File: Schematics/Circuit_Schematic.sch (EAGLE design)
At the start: 38 parts, among them Q1 L7812ACV, U1 TDA2822M, X1 1502_01

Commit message: added proper eagle parts for ram and custom part for DAC
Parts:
- removed 23LC1024: (no value), TDA2822D_Breakout:MA04-2
- removed UDA1334ATS: (no value), TDA2822D_Breakout:MA08-2
- added U2: 23LC1024-I/SN, microchip_fromOneCall:23LC1024-I/SN
- added UDA1334ATS/N2_ALEX1: UDA1334ATS/N2_ALEX, UDA1334ATS_ALEX:UDA1334ATS/N2_ALEX
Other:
- note added: "RAM"
- note removed: "RAM for DAC"
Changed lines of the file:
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@@
 <part name="R1" library="SparkFun-Resistors" deviceset="1OHM" device="-0603-1/10W-1%" value="300"/>
 <part name="S1" library="switch" deviceset="255SB" device=""/>
-<part name="UDA1334ATS" library="TDA2822D_Breakout" deviceset="MA08-2" device=""/>
-<part name="23LC1024" library="TDA2822D_Breakout" deviceset="MA04-2" device=""/>
+<part name="U2" library="microchip_fromOneCall" deviceset="23LC1024-I/SN" device=""/>
+<part name="UDA1334ATS/N2_ALEX1" library="UDA1334ATS_ALEX" deviceset="UDA1334ATS/N2_ALEX" device=""/>
 </parts>
 <sheets>
@@
 <text x="83.82" y="175.26" size="1.778" layer="91">3.3V Regulator</text>
 <text x="-15.24" y="-12.7" size="1.778" layer="91">3.3V</text>
-<text x="12.7" y="58.42" size="1.778" layer="91">DAC</text>
-<text x="48.26" y="58.42" size="1.778" layer="91">RAM for DAC</text>
+<text x="0" y="-43.18" size="1.778" layer="91">DAC</text>
+<text x="68.58" y="-45.72" size="1.778" layer="91">RAM</text>
 </plain>
 <instances>
@@
 <instance part="R1" gate="G$1" x="43.18" y="167.64" rot="R90"/>
 <instance part="S1" gate="1" x="5.08" y="187.96" rot="R270"/>
-<instance part="UDA1334ATS" gate="G$1" x="15.24" y="43.18"/>
-<instance part="23LC1024" gate="G$1" x="53.34" y="50.8"/>
+<instance part="U2" gate="A" x="81.28" y="-63.5"/>
+<instance part="UDA1334ATS/N2_ALEX1" gate="G$1" x="0" y="-50.8"/>
 </instances>
 <busses>

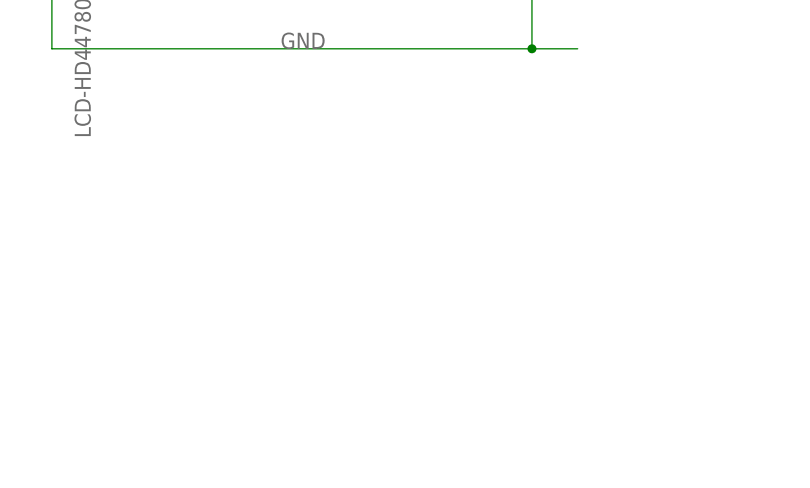
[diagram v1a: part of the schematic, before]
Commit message: Added EEPROM Chip 24C64
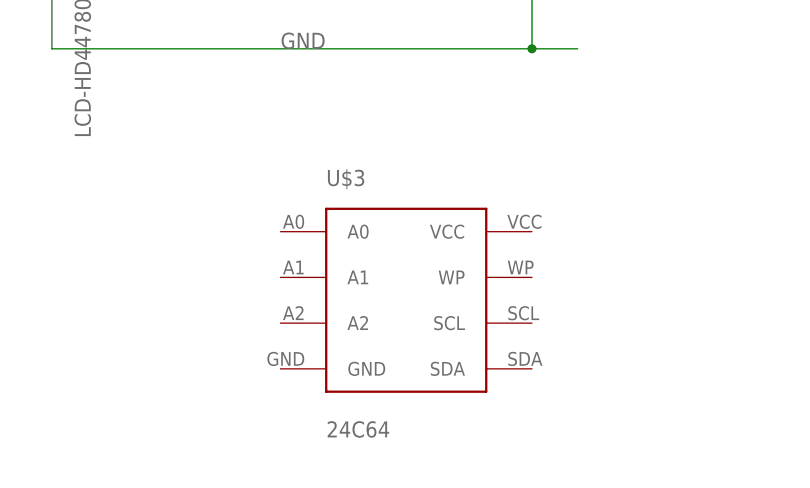
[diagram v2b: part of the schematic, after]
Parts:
- added U$3: 24C64, MIRO:24C64
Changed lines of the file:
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@@
 <part name="U2" library="microchip_fromOneCall" deviceset="23LC1024-I/SN" device=""/>
 <part name="UDA1334ATS/N2_ALEX1" library="UDA1334ATS_ALEX" deviceset="UDA1334ATS/N2_ALEX" device=""/>
+<part name="U$3" library="MIRO" deviceset="24C64" device=""/>
 </parts>
 <sheets>
@@
 <instance part="U2" gate="A" x="81.28" y="-63.5"/>
 <instance part="UDA1334ATS/N2_ALEX1" gate="G$1" x="0" y="-50.8"/>
+<instance part="U$3" gate="G$1" x="137.16" y="-81.28"/>
 </instances>
 <busses>

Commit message: Added ESP controls via NMOS transistors. Lil bit messy.
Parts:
- added T1, T2, T3, T4, T5: (no value), zetex:NMOSSOT223
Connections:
- removed net RD0: U$1.RD0/SEG0, U$2.DB0
- removed net RD1: U$1.RD1/SEG1, U$2.DB1
- new net N$22: MDL1.GPIO5, T1.G
- new net N$23: MDL1.GPIO4, T2.G
- new net N$26: MDL1.GPIO9, T3.G
- new net N$32: MDL1.GPIO12, T5.G
- net GND: now also T1.S, T2.S, T3.S, T4.S, T5.S
- net N$19: now also T2.D, U$1.RB1/INT1/SEG8; no longer U$1.RB5/KBI1
- net N$28: now also MDL1.GPIO10, T4.G; no longer U$1.RB1/INT1/SEG8, U$2.E
- net N$3: now also T5.D, U$1.RG1/TX2/CK2/SEG29; no longer U$1.RA0/AN0
- net N$33: now also T3.D
- net N$8: now also T1.D
- net VDD: now also T4.D, U$1.RG2/RX2/DT2/SEG28; no longer U$1.RA1/AN1
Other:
- note added: "Mute: RB0"
- note added: "Next Channel: RB1"
- note added: "Prev Channel: RB2"
- note added: "Vol Down: RB1"
- note added: "Vol Up: RB0"
- moved on the sheet: MDL1

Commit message: Added AR1010 chip to the schematic, got rid of the breakout for it
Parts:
- removed AR1010_BRKT: (no value), con-lstb:MA07-1
- added U$4: AR1010, MIRO:AR1010
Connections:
- removed net N$2: AR1010_BRKT.1, Q1.OUT
- removed net N$21: MDL1.VCC
- new net VCC: MDL1.VCC, U$4.VCC
- net CLOCK: now also U$4.SCL; no longer AR1010_BRKT.6
- net DATA: now also U$4.SDA; no longer AR1010_BRKT.7_DATA
- net GND: now also U$4.GND; no longer AR1010_BRKT.2
- net N$10: now also U$4.L-OUT; no longer AR1010_BRKT.3
- net N$13: now also U$4.R-OUT; no longer AR1010_BRKT.4
- net VDD: now also Q1.OUT
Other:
- note removed: "CLOCK"
- note removed: "DATA"
- note removed: "GND"
- note removed: "LEFT"
- note removed: "RIGHT"
- note removed: "VSS"
- note removed: "W/R"
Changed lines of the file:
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@@
 </classes>
 <parts>
-<part name="AR1010_BRKT" library="con-lstb" deviceset="MA07-1" device=""/>
 <part name="U1" library="ST Microelctronics_By_element14_Batch_1" deviceset="TDA2822M" device=""/>
 <part name="U$1" library="Microchip_By_element14_Batch_1" deviceset="PIC18F6490-I/PT" device=""/>
@@
 <part name="T4" library="zetex" deviceset="NMOSSOT223" device=""/>
 <part name="T5" library="zetex" deviceset="NMOSSOT223" device=""/>
+<part name="U$4" library="MIRO" deviceset="AR1010" device=""/>
 </parts>
 <sheets>
 <sheet>
 <plain>
-<text x="5.08" y="86.36" size="1.778" layer="91">DATA</text>
-<text x="5.08" y="83.82" size="1.778" layer="91">CLOCK</text>
-<text x="5.08" y="81.28" size="1.778" layer="91">W/R</text>
-<text x="5.08" y="78.74" size="1.778" layer="91">RIGHT</text>
-<text x="5.08" y="76.2" size="1.778" layer="91">LEFT</text>
-<text x="5.08" y="73.66" size="1.778" layer="91">GND</text>
-<text x="5.08" y="71.12" size="1.778" layer="91">VSS</text>
 <text x="83.82" y="175.26" size="1.778" layer="91">3.3V Regulator</text>
 <text x="358.14" y="45.72" size="1.778" layer="91">3.3V</text>
@@
 </plain>
 <instances>
-<instance part="AR1010_BRKT" gate="1" x="-5.08" y="78.74" smashed="yes">
-<attribute name="VALUE" x="-6.35" y="66.04" size="1.778" layer="96"/>
-<attribute name="NAME" x="-6.35" y="89.662" size="1.778" layer="95"/>
-</instance>
 <instance part="U1" gate="A" x="86.36" y="127"/>
 <instance part="U$1" gate="A" x="226.06" y="83.82"/>
@@
 <instance part="T4" gate="A" x="391.16" y="157.48"/>
 <instance part="T5" gate="A" x="391.16" y="172.72"/>
+<instance part="U$4" gate="G$1" x="-12.7" y="43.18"/>
 </instances>
 <busses>
 </busses>
 <nets>
-<net name="N$2" class="0">
-<segment>
-<pinref part="Q1" gate="A" pin="OUT"/>
-<wire x1="111.76" y1="167.64" x2="116.84" y2="167.64" width="0.1524" layer="91"/>
-<wire x1="116.84" y1="167.64" x2="116.84" y2="71.12" width="0.1524" layer="91"/>
-<pinref part="AR1010_BRKT" gate="1" pin="1"/>
-<wire x1="116.84" y1="71.12" x2="2.54" y2="71.12" width="0.1524" layer="91"/>
-</segment>
-</net>
 <net name="VDD" class="0">
 <segment>
@@
 <wire x1="312.42" y1="109.22" x2="317.5" y2="109.22" width="0.1524" layer="91"/>
 <label x="317.5" y="109.22" size="1.778" layer="95"/>
+</segment>
+<segment>
+<pinref part="Q1" gate="A" pin="OUT"/>
+<wire x1="111.76" y1="167.64" x2="116.84" y2="167.64" width="0.1524" layer="91"/>
+<label x="116.84" y="167.64" size="1.778" layer="95"/>
 </segment>
 </net>
@@
 <junction x="17.78" y="162.56"/>
 <junction x="-15.24" y="162.56"/>
+<label x="63.5" y="165.1" size="1.778" layer="95"/>
 </segment>
 <segment>
@@
 </segment>
 <segment>
-<pinref part="AR1010_BRKT" gate="1" pin="2"/>
-<wire x1="53.34" y1="73.66" x2="2.54" y2="73.66" width="0.1524" layer="91"/>
-</segment>
-<segment>
 <wire x1="180.34" y1="-48.26" x2="175.26" y2="-48.26" width="0.1524" layer="91"/>
 <junction x="175.26" y="-48.26"/>
@@
 <label x="408.94" y="45.72" size="1.778" layer="95"/>
 </segment>
+<segment>
+<pinref part="U$4" gate="G$1" pin="GND"/>
+<wire x1="30.48" y1="33.02" x2="40.64" y2="33.02" width="0.1524" layer="91"/>
+<label x="39" y="34" size="1.778" layer="95"/>
+</segment>
 </net>
 <net name="N$1" class="0">
@@
 <net name="N$10" class="0">
 <segment>
-<pinref part="AR1010_BRKT" gate="1" pin="3"/>
 <pinref part="C4" gate="G$1" pin="2"/>
-<wire x1="2.54" y1="76.2" x2="33.02" y2="76.2" width="0.1524" layer="91"/>
-<wire x1="33.02" y1="76.2" x2="33.02" y2="83.82" width="0.1524" layer="91"/>
+<pinref part="U$4" gate="G$1" pin="L-OUT"/>
+<wire x1="30.48" y1="43.18" x2="33.02" y2="43.18" width="0.1524" layer="91"/>
+<wire x1="33.02" y1="43.18" x2="33.02" y2="83.82" width="0.1524" layer="91"/>
 </segment>
 </net>
@@
 <segment>
 <pinref part="C3" gate="G$1" pin="2"/>
-<wire x1="45.72" y1="83.82" x2="45.72" y2="78.74" width="0.1524" layer="91"/>
-<pinref part="AR1010_BRKT" gate="1" pin="4"/>
-<wire x1="45.72" y1="78.74" x2="2.54" y2="78.74" width="0.1524" layer="91"/>
+<wire x1="45.72" y1="83.82" x2="45.72" y2="38.1" width="0.1524" layer="91"/>
+<pinref part="U$4" gate="G$1" pin="R-OUT"/>
+<wire x1="45.72" y1="38.1" x2="30.48" y2="38.1" width="0.1524" layer="91"/>
 </segment>
 </net>
@@
 <net name="DATA" class="0">
 <segment>
-<pinref part="AR1010_BRKT" gate="1" pin="7_DATA"/>
-<wire x1="2.54" y1="86.36" x2="17.78" y2="86.36" width="0.1524" layer="91"/>
-</segment>
-<segment>
 <pinref part="U$1" gate="A" pin="RC4/SDI/SDA"/>
 <wire x1="269.24" y1="99.06" x2="276.86" y2="99.06" width="0.1524" layer="91"/>
 <label x="271.78" y="99.06" size="1.778" layer="95"/>
 </segment>
+<segment>
+<pinref part="U$4" gate="G$1" pin="SDA"/>
+<wire x1="-2.54" y1="53.34" x2="-12.7" y2="53.34" width="0.1524" layer="91"/>
+<label x="-12.7" y="53.34" size="1.778" layer="95"/>
+</segment>
 </net>
 <net name="CLOCK" class="0">
-<segment>
-<pinref part="AR1010_BRKT" gate="1" pin="6"/>
-<wire x1="2.54" y1="83.82" x2="17.78" y2="83.82" width="0.1524" layer="91"/>
-</segment>
 <segment>
 <pinref part="U$1" gate="A" pin="RC3/SCK/SCL"/>
 <wire x1="269.24" y1="101.6" x2="276.86" y2="101.6" width="0.1524" layer="91"/>
 <label x="271.78" y="101.6" size="1.778" layer="95"/>
+</segment>
+<segment>
+<pinref part="U$4" gate="G$1" pin="SCL"/>
+<wire x1="-2.54" y1="48.26" x2="-12.7" y2="48.26" width="0.1524" layer="91"/>
+<label x="-12.7" y="48.26" size="1.778" layer="95"/>
 </segment>
 </net>
@@
 <pinref part="S1" gate="1" pin="P"/>
 <wire x1="-5.08" y1="185.42" x2="0" y2="185.42" width="0.1524" layer="91"/>
-</segment>
-</net>
-<net name="N$21" class="0">
-<segment>
-<pinref part="MDL1" gate="G$1" pin="VCC"/>
-<wire x1="370.84" y1="45.72" x2="363.22" y2="45.72" width="0.1524" layer="91"/>
 </segment>
 </net>
@@
 <segment>
 <pinref part="T5" gate="A" pin="G"/>
+<wire x1="386.08" y1="170.18" x2="365.76" y2="170.18" width="0.1524" layer="91"/>
 <pinref part="MDL1" gate="G$1" pin="GPIO12"/>
-<wire x1="386.08" y1="170.18" x2="365.76" y2="165.1" width="0.1524" layer="91"/>
-<wire x1="365.76" y1="165.1" x2="370.84" y2="50.8" width="0.1524" layer="91"/>
-</segment>
-</net>
+<wire x1="370.84" y1="50.8" x2="365.76" y2="50.8" width="0.1524" layer="91"/>
+<wire x1="365.76" y1="50.8" x2="365.76" y2="170.18" width="0.1524" layer="91"/>
+</segment>
+</net>
+<net name="VCC" class="0">
+<segment>
+<pinref part="U$4" gate="G$1" pin="VCC"/>
+<wire x1="-2.54" y1="33.02" x2="-12.7" y2="33.02" width="0.1524" layer="91"/>
+<label x="-13" y="34" size="1.778" layer="95"/>
+</segment>
+<segment>
+<pinref part="MDL1" gate="G$1" pin="VCC"/>
+<wire x1="370.84" y1="45.72" x2="363.22" y2="45.72" width="0.1524" layer="91"/>
+</segment>
+</net>

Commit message: tidied up schematic a bit
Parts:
- removed Q1: L7812ACV, ST Microelctronics_By_element14_Batch_1:L7812ACV
- added Q2: LE33CZ, ST Microelctronics_By_element14_Batch_1:LE33CZ
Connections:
- new net 3.3V: MDL1.VCC, Q2.VOUT
- net GND: now also Q2.GND; no longer Q1.GND
- net VCC: no longer MDL1.VCC
- net VDD: now also Q2.VIN; no longer Q1.IN, Q1.OUT
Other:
- note removed: "3.3V Regulator"
- moved on the sheet: R10, R5, R7, R8, R9, S2, S3, S4, S5, S6, T1, T2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
